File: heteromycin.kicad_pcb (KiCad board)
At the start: 4 copper layers, 200 x 100 mm, 374 parts, among them J1 M20-7832046, J10 DM3D-SF, J11 20021121-00010C4LF, J12 70543-0001, J13 70543-0001, J14 70543-0001, J15 70543-0001, J16 70543-0001, J17 70543-0001, J18 70543-0001, J19 70543-0001, J2 4DB-P108-06, J20 70543-0003, J21 70543-0002, J22 70543-0002, J23 70543-0002, J24 Conn_02x20_Odd_Even, J25 Conn_02x03_Counter_Clockwise, J3 39531-1002, J4 39531-1002, J5 70543-0003, J6 70543-0003, J7 70543-0003, J8 70543-0003, J9 70543-0003, Q1 DMMT5401, Q10 IRLML0030TRPbF, Q11 IRLML0030TRPbF, Q12 PSMN1R2-30YLC,115, Q13 PSMN1R2-30YLC,115, Q14 PSMN1R2-30YLC,115, Q15 IRLML0030TRPbF, Q16 IRLML0030TRPbF, Q17 IRLML0030TRPbF, Q18 IRLML0030TRPbF, Q19 IRLML0030TRPbF, Q2 DMG2305UX, Q20 IRLML0030TRPbF, Q21 IRLML0030TRPbF, Q22 IRLML0030TRPbF, Q23 IRLML0030TRPbF, Q24 IRLML0030TRPbF, Q25 IRLML0030TRPbF, Q26 IRLML0030TRPbF, Q27 IRLML0030TRPbF, Q28 IRLML0030TRPbF, Q29 IRLML0030TRPbF, Q3 MMBT3904-7-F, Q30 IRLML0030TRPbF, Q31 IRLML0030TRPbF, Q32 IRLML0030TRPbF, Q33 IRLML0030TRPbF, Q34 IRLML0030TRPbF, Q35 IRLML0030TRPbF, Q36 IRLML0030TRPbF, Q37 IRLML0030TRPbF, Q38 IRLML0030TRPbF, Q39 IRLML0030TRPbF, Q4 IRLML0030TRPbF, Q40 IRLML0030TRPbF, Q41 IRLML0030TRPbF, Q42 IRLML0030TRPbF, Q43 IRLML0030TRPbF, Q44 IRLML0030TRPbF, Q45 IRLML0030TRPbF, Q46 IRLML0030TRPbF, Q47 IRLML0030TRPbF, Q48 IRLML0030TRPbF, Q49 IRLML0030TRPbF, Q5 IRLML0030TRPbF, Q50 IRLML0030TRPbF, Q6 IRLML0030TRPbF, Q7 IRLML0030TRPbF, Q8 IRLML0030TRPbF, Q9 IRLML0030TRPbF, SW1 PTS645VL39-2, U1 CAT24C32, U10 TMC2160-TA, U2 i3A, U3 AP7365-33WG-7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

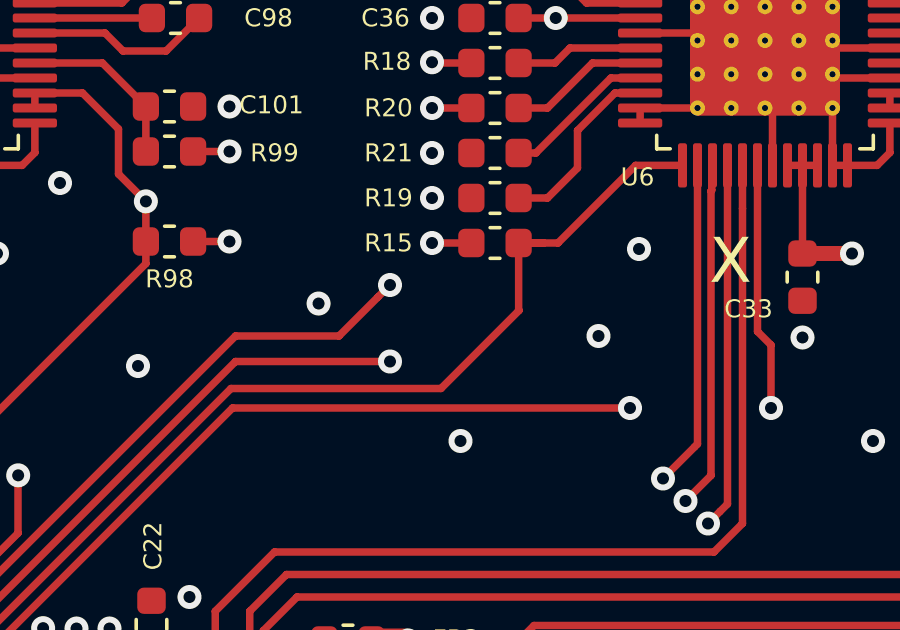
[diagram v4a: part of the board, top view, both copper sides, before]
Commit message: Updated image and added some copper pour
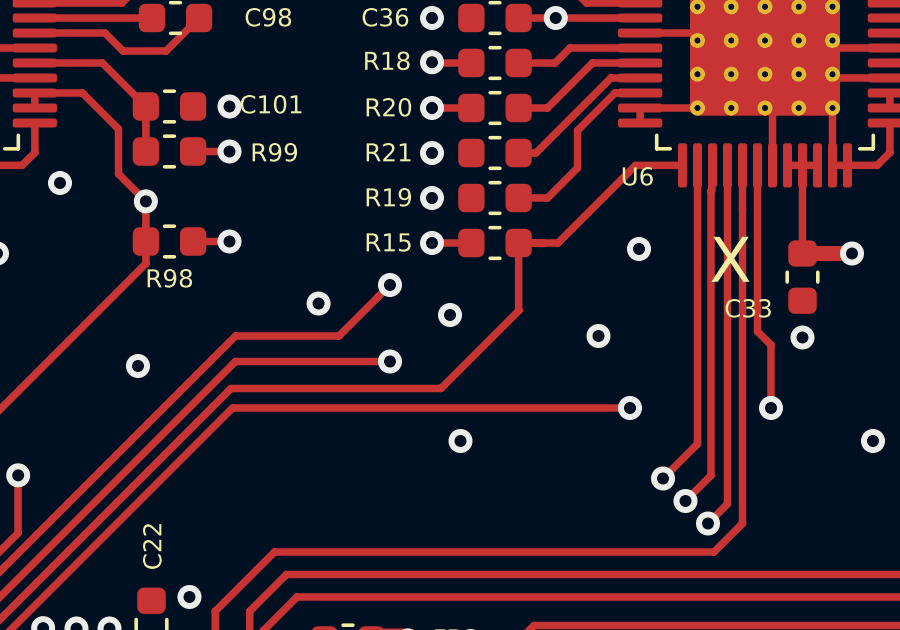
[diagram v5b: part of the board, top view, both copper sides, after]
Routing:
- net GND: vias 325 -> 326
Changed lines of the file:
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@@
     (thickness 1.6)
     (drawings 81)
-    (tracks 4060)
+    (tracks 4061)
     (zones 0)
     (modules 374)
@@
   (via (at 162.4 82.8) (size 0.8) (drill 0.4) (layers F.Cu B.Cu) (net 4))
   (via (at 190.7 89.4) (size 0.8) (drill 0.4) (layers F.Cu B.Cu) (net 4))
+  (via (at 118.4 87.3) (size 0.8) (drill 0.4) (layers F.Cu B.Cu) (net 4))
   (via (at 103.3 85.25) (size 0.8) (drill 0.4) (layers F.Cu B.Cu) (net 5))
   (segment (start 103.3 85.25) (end 101.65 85.25) (width 0.5) (layer F.Cu) (net 5))

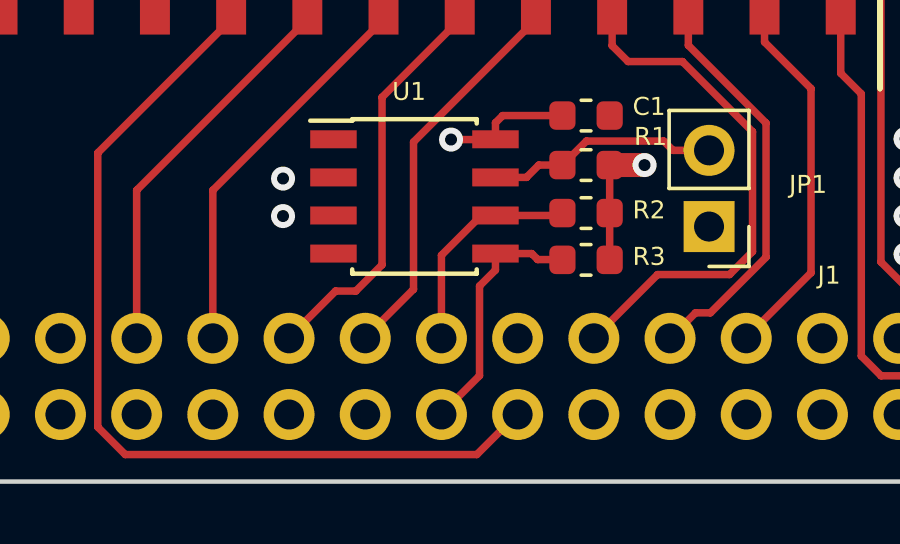
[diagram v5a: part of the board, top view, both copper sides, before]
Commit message: Switched EEPROM I2C traces for the RPI
SDA and SCL were switched. Also some formatting for the
EEPROM settings.txt.
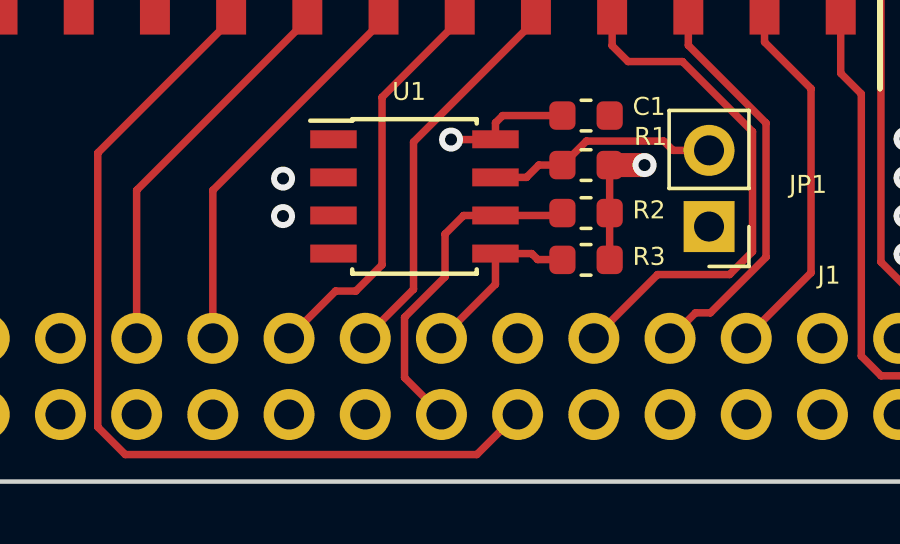
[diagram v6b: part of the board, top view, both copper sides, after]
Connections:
- R2 pad 2: /Raspberry Pi Connector/ID_SD_EEPROM -> /Raspberry Pi Connector/ID_SC_EEPROM
- R3 pad 2: /Raspberry Pi Connector/ID_SC_EEPROM -> /Raspberry Pi Connector/ID_SD_EEPROM
- U1 pad 5: /Raspberry Pi Connector/ID_SC_EEPROM -> /Raspberry Pi Connector/ID_SD_EEPROM
- U1 pad 6: /Raspberry Pi Connector/ID_SD_EEPROM -> /Raspberry Pi Connector/ID_SC_EEPROM
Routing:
- net /Raspberry Pi Connector/ID_SC_EEPROM: track 8.42 -> 11.8 mm
- net /Raspberry Pi Connector/ID_SD_EEPROM: track 7.40 -> 5.90 mm
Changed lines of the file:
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@@
-(kicad_pcb (version 20171130) (host pcbnew 5.0.1-33cea8e~68~ubuntu18.10.1)
+(kicad_pcb (version 20171130) (host pcbnew 5.0.2-bee76a0~70~ubuntu18.10.1)
   (general
     (thickness 1.6)
     (drawings 81)
-    (tracks 4061)
+    (tracks 4063)
     (zones 0)
     (modules 374)
@@
       (net 4 GND))
     (pad 5 smd rect (at 2.7 1.905) (size 1.55 0.6) (layers F.Cu F.Paste F.Mask)
-      (net 8 "/Raspberry Pi Connector/ID_SC_EEPROM"))
-    (pad 6 smd rect (at 2.7 0.635) (size 1.55 0.6) (layers F.Cu F.Paste F.Mask)
       (net 6 "/Raspberry Pi Connector/ID_SD_EEPROM"))
+    (pad 6 smd rect (at 2.7 0.635) (size 1.55 0.6) (layers F.Cu F.Paste F.Mask)
+      (net 8 "/Raspberry Pi Connector/ID_SC_EEPROM"))
     (pad 7 smd rect (at 2.7 -0.635) (size 1.55 0.6) (layers F.Cu F.Paste F.Mask)
       (net 9 "Net-(JP1-Pad2)"))
@@
     (fp_line (start -0.8 0.4) (end -0.8 -0.4) (layer F.Fab) (width 0.1))
     (pad 2 smd roundrect (at 0.7875 0 180) (size 0.875 0.95) (layers F.Cu F.Paste F.Mask) (roundrect_rratio 0.25)
-      (net 8 "/Raspberry Pi Connector/ID_SC_EEPROM"))
+      (net 6 "/Raspberry Pi Connector/ID_SD_EEPROM"))
     (pad 1 smd roundrect (at -0.7875 0 180) (size 0.875 0.95) (layers F.Cu F.Paste F.Mask) (roundrect_rratio 0.25)
       (net 5 VDD3V3))
@@
       (net 5 VDD3V3))
     (pad 2 smd roundrect (at 0.7875 0 180) (size 0.875 0.95) (layers F.Cu F.Paste F.Mask) (roundrect_rratio 0.25)
-      (net 6 "/Raspberry Pi Connector/ID_SD_EEPROM"))
+      (net 8 "/Raspberry Pi Connector/ID_SC_EEPROM"))
     (model ${KISYS3DMOD}/Resistor_SMD.3dshapes/R_0603_1608Metric.wrl
       (at (xyz 0 0 0))
@@
   (segment (start 188.8 92) (end 190.3 92) (width 0.25) (layer F.Cu) (net 5))
   (segment (start 190.3 92) (end 190.65 91.65) (width 0.25) (layer F.Cu) (net 5))
-  (segment (start 89.90591 141.130559) (end 88.58 142.456469) (width 0.25) (layer F.Cu) (net 6) (status 10))
-  (segment (start 88.58 142.456469) (end 88.58 145.2) (width 0.25) (layer F.Cu) (net 6) (status 20))
-  (segment (start 90.38091 141.130559) (end 89.90591 141.130559) (width 0.25) (layer F.Cu) (net 6) (status 30))
-  (segment (start 92.581941 141.130559) (end 92.6125 141.1) (width 0.25) (layer F.Cu) (net 6))
-  (segment (start 92.531941 141.130559) (end 92.6125 141.05) (width 0.25) (layer F.Cu) (net 6))
-  (segment (start 90.38091 141.130559) (end 92.531941 141.130559) (width 0.25) (layer F.Cu) (net 6))
+  (segment (start 90.382542 142.398927) (end 90.38091 142.400559) (width 0.25) (layer F.Cu) (net 6) (status 30))
+  (segment (start 91.79 142.6) (end 92.628675 142.6) (width 0.25) (layer F.Cu) (net 6))
+  (segment (start 90.38091 142.400559) (end 91.590559 142.400559) (width 0.25) (layer F.Cu) (net 6))
+  (segment (start 91.590559 142.400559) (end 91.79 142.6) (width 0.25) (layer F.Cu) (net 6))
+  (segment (start 90.38091 143.42409) (end 90.38091 142.400559) (width 0.25) (layer F.Cu) (net 6))
+  (segment (start 88.58 145.225) (end 90.38091 143.42409) (width 0.25) (layer F.Cu) (net 6))
   (segment (start 122.82628 138.206706) (end 122.87628 138.156706) (width 0.25) (layer F.Cu) (net 7) (status 30))
   (segment (start 122.82628 139.853775) (end 122.82628 138.206706) (width 0.25) (layer F.Cu) (net 7) (status 30))
   (segment (start 122.82818 139.855675) (end 122.82628 139.853775) (width 0.25) (layer F.Cu) (net 7) (status 30))
   (segment (start 124.485622 139.855675) (end 122.82818 139.855675) (width 0.25) (layer F.Cu) (net 7) (status 30))
-  (segment (start 90.382542 142.398927) (end 90.38091 142.400559) (width 0.25) (layer F.Cu) (net 8) (status 30))
-  (segment (start 89.85 143.481469) (end 90.38091 142.950559) (width 0.25) (layer F.Cu) (net 8))
-  (segment (start 88.58 147.74) (end 89.85 146.47) (width 0.25) (layer F.Cu) (net 8) (status 10))
-  (segment (start 90.38091 142.950559) (end 90.38091 142.400559) (width 0.25) (layer F.Cu) (net 8) (status 20))
-  (segment (start 89.85 146.47) (end 89.85 143.481469) (width 0.25) (layer F.Cu) (net 8))
-  (segment (start 91.79 142.6) (end 92.628675 142.6) (width 0.25) (layer F.Cu) (net 8))
-  (segment (start 90.38091 142.400559) (end 91.590559 142.400559) (width 0.25) (layer F.Cu) (net 8))
-  (segment (start 91.590559 142.400559) (end 91.79 142.6) (width 0.25) (layer F.Cu) (net 8))
+  (segment (start 90.38091 141.130559) (end 89.90591 141.130559) (width 0.25) (layer F.Cu) (net 8) (status 30))
+  (segment (start 92.581941 141.130559) (end 92.6125 141.1) (width 0.25) (layer F.Cu) (net 8))
+  (segment (start 92.531941 141.130559) (end 92.6125 141.05) (width 0.25) (layer F.Cu) (net 8))
+  (segment (start 90.38091 141.130559) (end 92.531941 141.130559) (width 0.25) (layer F.Cu) (net 8))
+  (segment (start 89.319441 141.130559) (end 90.38091 141.130559) (width 0.25) (layer F.Cu) (net 8))
+  (segment (start 88.7 143.17641) (end 88.7 141.75) (width 0.25) (layer F.Cu) (net 8))
+  (segment (start 87.35 144.52641) (end 88.7 143.17641) (width 0.25) (layer F.Cu) (net 8))
+  (segment (start 88.7 141.75) (end 89.319441 141.130559) (width 0.25) (layer F.Cu) (net 8))
+  (segment (start 88.58 147.765) (end 87.35 146.535) (width 0.25) (layer F.Cu) (net 8))
+  (segment (start 87.35 146.535) (end 87.35 144.52641) (width 0.25) (layer F.Cu) (net 8))
   (segment (start 91.415425 139.860559) (end 90.38091 139.860559) (width 0.25) (layer F.Cu) (net 9))
   (segment (start 92.6125 139.45) (end 91.825984 139.45) (width 0.25) (layer F.Cu) (net 9))
